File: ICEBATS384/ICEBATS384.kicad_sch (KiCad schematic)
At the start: 10 parts, among them J1 513389873, J2 5017450401, U4 NCP114AMX120TCG, Y1 ASCO

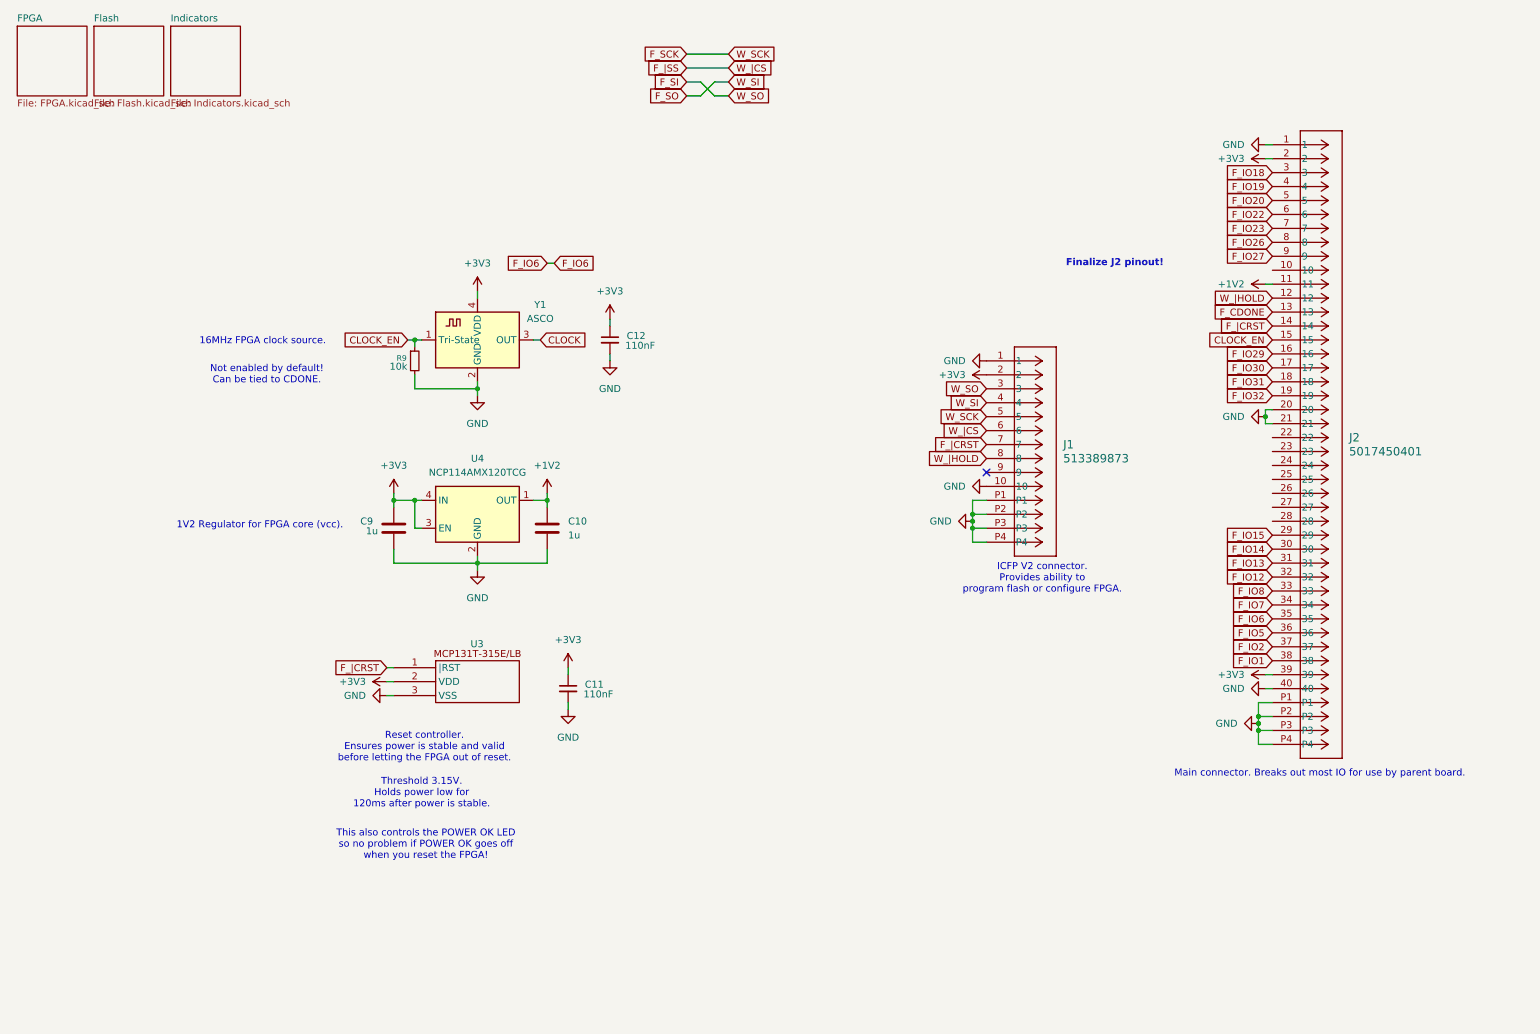
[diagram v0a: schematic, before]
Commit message: Fixes missing schematic connections.
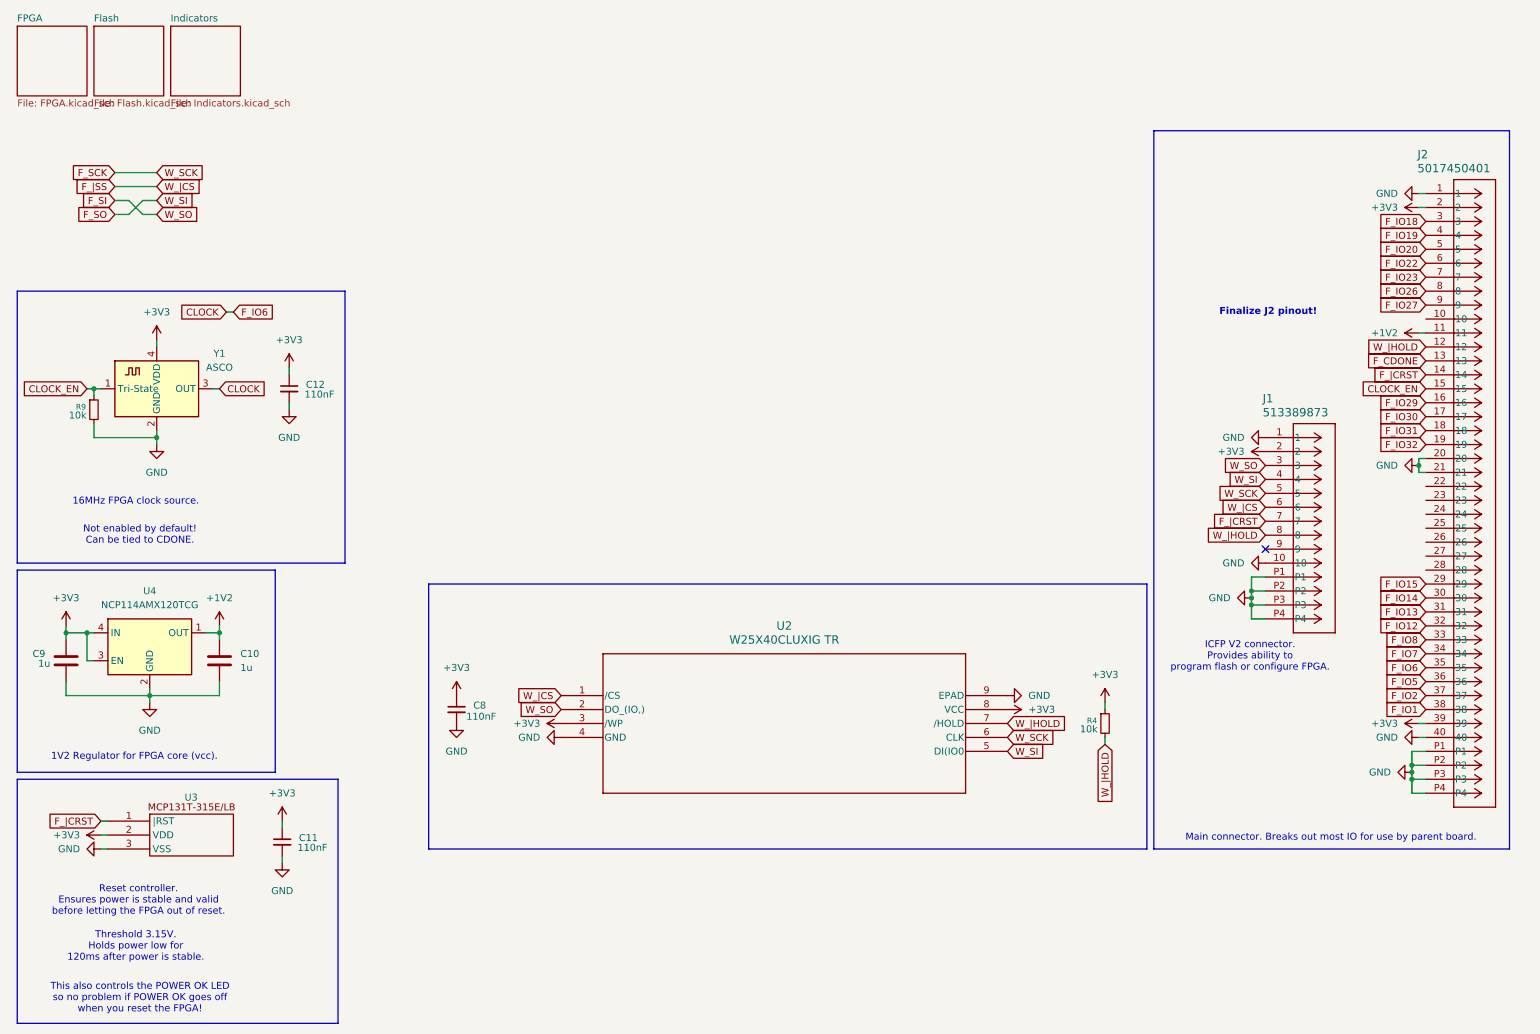
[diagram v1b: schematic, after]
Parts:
- added C8: 110nF, Capacitor_SMD:C_0402_1005Metric, symbol Device:C_Small
- added R4: 10k, Resistor_SMD:R_0402_1005Metric, symbol Device:R_Small
- added U2: W25X40CLUXIG TR, Package_SON:Winbond_USON-8-1EP_3x2mm_P0.5mm_EP0.2x1.6mm, symbol 2025-06-09_04-19-34:W25X40CLUXIG_TR
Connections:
- net F_IO6 is gone; now on net CLOCK: J2.35
- net +3V3: now also C8.1, R4.1, U2.3 (/WP), U2.8 (VCC)
- net F_SCK: now also U2.6 (CLK)
- net F_SI: now also U2.2 (DO_(IO,))
- net F_SO: now also U2.5 (DI(IO0)
- net F_|SS: now also U2.1 (/CS)
- net GND: now also C8.2, U2.4 (GND), U2.9 (EPAD)
- net W_|HOLD: now also R4.2, U2.7 (/HOLD)
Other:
- moved on the sheet: C10, C11, C12, C9, J1, J2, R9, U3, U4, Y1

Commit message: Sheet documentation
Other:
- removed sheet Flash
- company: (none) -> Soldersplash
- title: (none) -> ICEBATS384
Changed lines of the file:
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@@
 	(generator_version "9.0")
 	(paper "A4")
+	(title_block
+		(title "ICEBATS384")
+		(date "2025-06-13")
+		(rev "A")
+		(company "Soldersplash")
+	)
